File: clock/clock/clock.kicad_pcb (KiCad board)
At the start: 2 copper layers, 43 parts, among them J1 AVR-ISP-6, J10 Conn_01x05_Male, J11 Conn_01x05_Male, J12 Conn_01x05_Male, J13 Conn_01x05_Male, J2 EURORACK_CONN_10, J3 CV_IN, J4 CLOCK_OUT, J5 SUBDIV_OUT, J6 Conn_01x05_Female, J7 Conn_01x05_Female, J8 Conn_01x05_Female, J9 Conn_01x05_Female, SW1 SW_Push, SW2 SW_Push, SW3 SW_Rotary8, U1 ATmega328P-PU, U2 L7805, U3 SM460281N, U4 SM460281N, U5 SM460281N, Y1 16MHz

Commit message: pcb layout first pass
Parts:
- removed the J10 at (1.91, 32.4)
- removed the J11 at (1.91, 46.4)
- removed the J12 at (1.91, 60.3)
- added J3: Conn_01x05_Female, Connector_PinSocket_2.54mm:PinSocket_1x05_P2.54mm_Vertical, F.Cu at (42.0, 33.5)
- added J4: Conn_01x05_Male, Connector_PinHeader_2.54mm:PinHeader_1x05_P2.54mm_Vertical, B.Cu at (2.00, 33.5)
- added J5: Conn_01x05_Female, Connector_PinSocket_2.54mm:PinSocket_1x05_P2.54mm_Vertical, F.Cu at (42.0, 48.8)
- J6, J8: value Conn_01x05_Female -> Conn_01x05_Male; footprint Connector_PinSocket_2.54mm:PinSocket_1x05_P2.54mm_Vertical -> Connector_PinHeader_2.54mm:PinHeader_1x05_P2.54mm_Vertical; moved to B.Cu
- moved R5 113.7 mm to (7.49, 100.7), turned to 180 degrees
- moved R4 111.0 mm to (13.0, 100.7), turned to 180 degrees
- moved C3 70.2 mm to (42.5, 25.0), turned to 270 degrees
- moved C1 64.4 mm to (43.0, 80.8), turned to 90 degrees
- moved J1 62.5 mm to (52.8, 84.0)
- moved R15 62.2 mm to (46.5, 38.0)
- moved R14 58.9 mm to (46.5, 34.5)
- moved R13 56.3 mm to (46.5, 31.0)
- moved C4 53.9 mm to (48.5, 27.0)
- moved J9 49.4 mm to (42.0, 97.8)
- moved J8 48.5 mm to (2.00, 64.0), turned to 180 degrees
- moved R1 41.7 mm to (42.0, 84.0)
- moved C2 40.9 mm to (52.8, 79.2), turned to 180 degrees
- moved U1 39.0 mm to (45.5, 41.5)
- moved Y1 37.6 mm to (52.5, 33.0), turned to 270 degrees
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- renumbered J13 to J10, J3 to J11, J4 to J12, J5 to J13
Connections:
- J10 pad 3: /LED_A -> /AVCC
- J10 pad 4: /LED_B -> /AGND
- J13 pad S: /AGND -> Net-(J13-PadS)
- J6 pad 1: /B_CLOCK_OUT -> /LED2
- J6 pad 2: /B_SUBDIV_OUT -> /LED_C2
- J6 pad 3: /B_CV_IN -> /LED1
- J6 pad 4: /B_LED0 -> /LED3
- J6 pad 5: /B_LED1 -> /LED_C3
- J7 pad 1: /B_LED2 -> /B_LED4
- J7 pad 2: /B_LED3 -> /B_LED5
- J7 pad 3: /B_LED4 -> /B_LED6
- J7 pad 4: /B_LED5 -> /B_LED_A
- J7 pad 5: /B_LED6 -> /B_LED_B
- J8 pad 1: /B_LED_C1 -> /LED4
- J8 pad 2: /B_LED_C2 -> /LED5
- J8 pad 3: /B_LED_C3 -> /LED6
- J8 pad 4: +5V -> /LED_A
- J8 pad 5: GND -> /LED_B
- J9 pad 3: /B_LED_A -> +5V
- J9 pad 4: /B_LED_B -> GND
- R4 pad 2: GND -> /AGND
- R5 pad 2: GND -> /AGND
- U4 pad 2: /LED1 -> /LED2
- U4 pad 4: /LED2 -> /LED1
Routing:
- net /B_SUBDIV_OUT: track 0.00 -> 76.2 mm, vias 0 -> 1
- net +5V: track 0.00 -> 71.3 mm
- net /B_KNOB: track 0.00 -> 52.2 mm
- net /B_CLOCK_OUT: track 0.00 -> 51.6 mm
- net /~RESET: track 0.00 -> 51.6 mm, vias 0 -> 1
- net /LED_A: track 0.00 -> 46.3 mm
- net Net-(C3-Pad2): track 0.00 -> 44.2 mm
- net /B_SW2: track 0.00 -> 43.8 mm
- net Net-(C4-Pad2): track 0.00 -> 41.3 mm
- net /AVCC: track 57.4 -> 97.7 mm
- net /B_LED_A: track 0.00 -> 37.1 mm
- net /LED_B: track 0.00 -> 35.8 mm
- net /B_SW1: track 0.00 -> 29.2 mm
- net /LED1: track 4.00 -> 28.6 mm
- net /LED2: track 4.23 -> 28.8 mm
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- added copper zone on B.Cu, net GND
- added copper zone on F.Cu, net GND
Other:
- board text added: "TODO: power connector orientation?"
- board text added: "TODO: silkscreen"
- board text added: "TODO: switch connector sides for stability?"

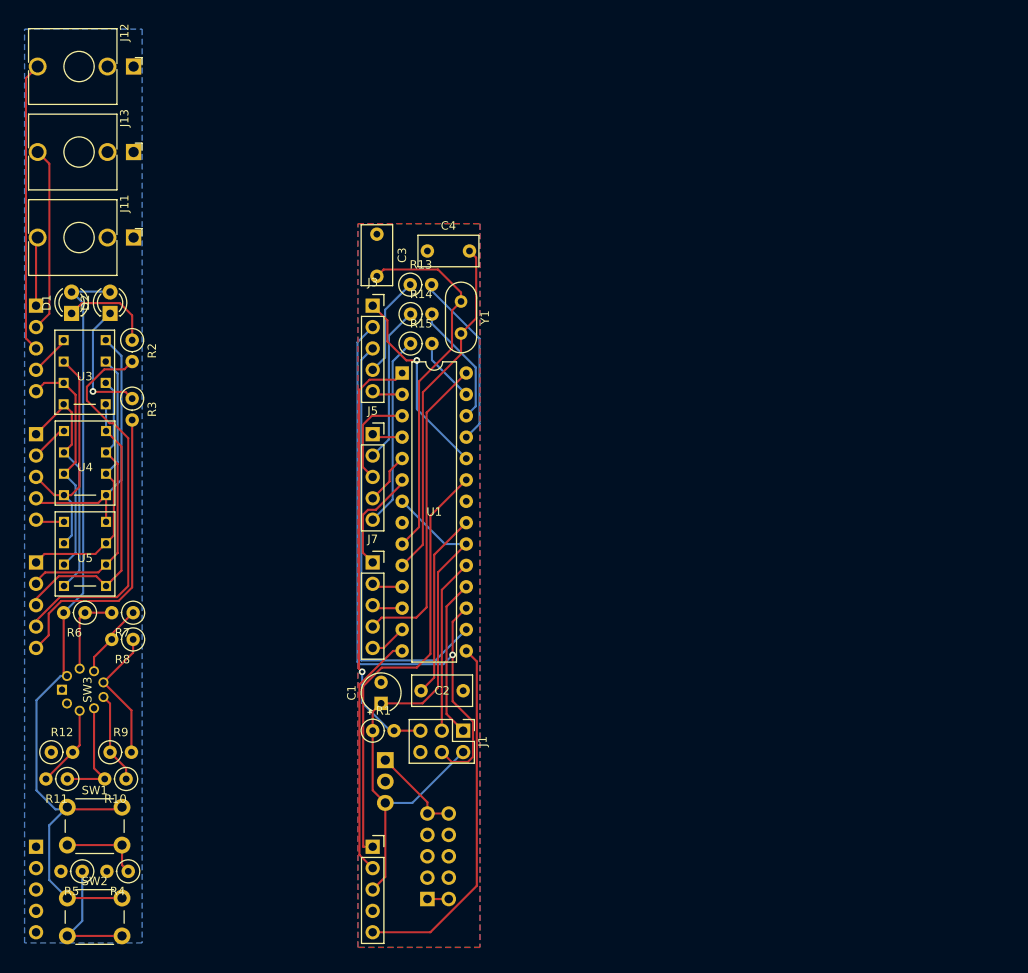
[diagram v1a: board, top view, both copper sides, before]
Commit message: cleanup pcb and silkscreen
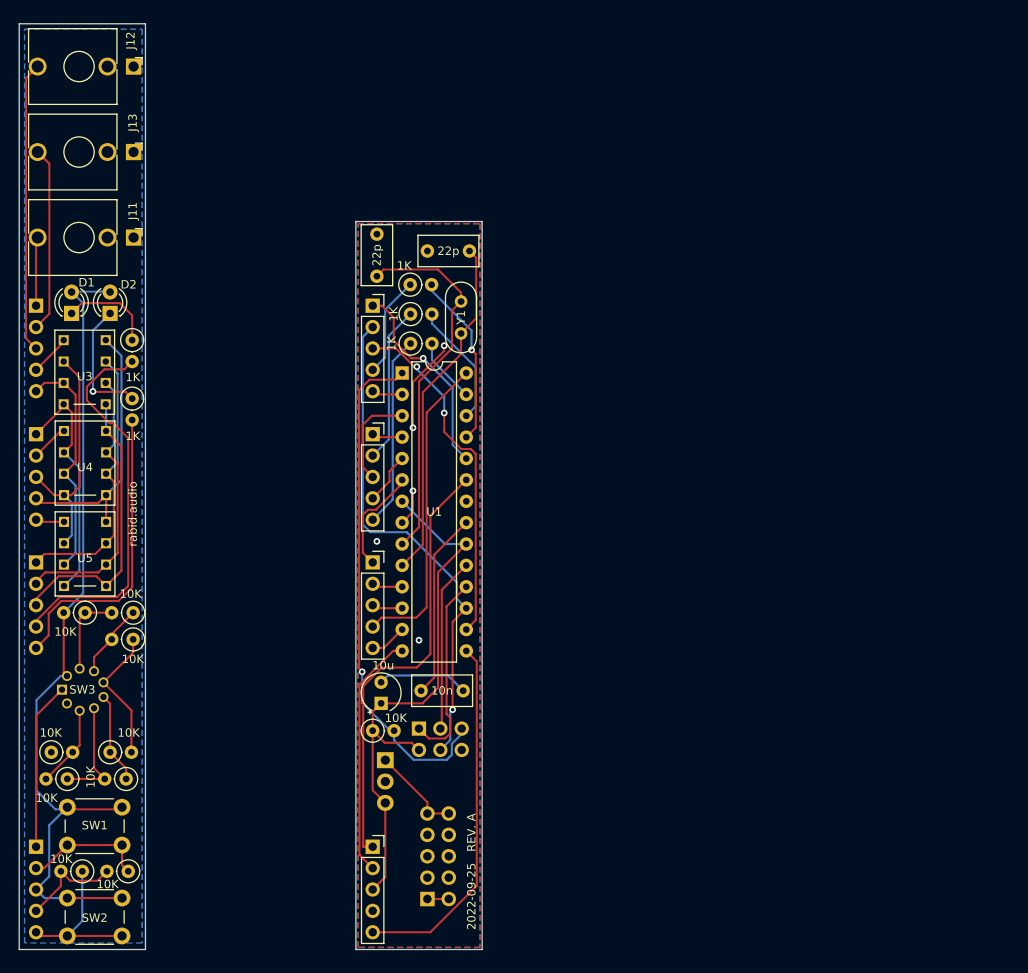
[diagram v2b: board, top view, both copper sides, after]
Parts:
- J1: value AVR-ISP-6 -> AVR-ISP; moved to B.Cu
- moved J1 5.26 mm to (47.5, 83.8)
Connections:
- J11 pad TN: (no net) -> /AGND
- J12 pad TN: (no net) -> Net-(J12-PadTN)
- J13 pad S: Net-(J13-PadS) -> /AGND
- J13 pad TN: (no net) -> Net-(J13-PadTN)
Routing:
- net GND: track 0.00 -> 26.4 mm, vias 0 -> 5
- net /KNOB: track 0.00 -> 19.9 mm
- net /B_SUBDIV_OUT: track 76.2 -> 59.6 mm
- net /AGND: track 0.00 -> 12.3 mm
- net /B_CLOCK_OUT: track 51.6 -> 41.4 mm, vias 0 -> 2
- net /~RESET: track 51.6 -> 61.2 mm
- net +5V: track 71.3 -> 66.0 mm
- net /SW1: track 9.93 -> 14.8 mm
- net /MISO: track 18.9 -> 23.0 mm
- net /SW2: track 15.5 -> 19.4 mm
- net /AVCC: track 97.7 -> 100.5 mm
- net /B_CV_IN: track 24.2 -> 24.9 mm
- net Net-(R13-Pad2): track 21.1 -> 20.8 mm, vias 0 -> 1
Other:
- board outline added: 55 x 110 mm
- board text added: "2022-09-25 REV. A"
- board text added: "TODO: confirm pot orientation"
- board text added: "TODO: confirm switches"
- board text added: "rabid.audio"
- board text removed: "TODO: silkscreen"

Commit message: update pcb
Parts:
- removed the R6 at (7.82, 70.0)
- removed the R8 at (13.5, 73.2)
- added D3: 1N4148, Diode_THT:D_T-1_P5.08mm_Horizontal, B.Cu at (7.33, 18.5)
- added R13: 68k, Resistor_THT:R_Axial_DIN0207_L6.3mm_D2.5mm_P2.54mm_Vertical, F.Cu at (5.25, 89.2)
- added R15: 100K, Resistor_THT:R_Axial_DIN0207_L6.3mm_D2.5mm_P7.62mm_Horizontal, B.Cu at (6.00, 22.0)
- J1: value AVR-ISP -> AVR-ISP-6
- R10: value 10K -> 220K
- R11: value 10K -> 470K
- R12: value 10K -> 1M
- R14: value 1K -> 180K; footprint Resistor_THT:R_Axial_DIN0207_L6.3mm_D2.5mm_P2.54mm_Vertical -> Resistor_THT:R_Axial_DIN0207_L6.3mm_D2.5mm_P7.62mm_Horizontal; moved to B.Cu
- R7: value 10K -> 1K
- R9: value 10K -> 120K
- SW3: value SW_Rotary8 -> SW_Coded_SH-7050; footprint synth:RM100772BCB -> synth:SD-1110
- moved R7 48.4 mm to (46.5, 34.5), turned to 0 degrees
- moved R14 37.1 mm to (9.87, 28.8), turned to 180 degrees
- moved R10 18.1 mm to (11.0, 71.8), turned to 270 degrees
- moved R12 15.1 mm to (6.50, 71.8), turned to 270 degrees
- moved R9 11.2 mm to (2.00, 93.5), turned to 90 degrees
- moved R11 7.30 mm to (13.0, 89.2)
- moved R8 6.75 mm to (46.5, 31.2)
- moved R6 6.75 mm to (46.5, 37.8)
- moved SW3 2.62 mm to (7.75, 81.8), turned to 0 degrees
- renumbered R13 to R6, R15 to R8
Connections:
- J11 pad T: /CV_IN -> Net-(D3-Pad2)
- R10 pad 1: Net-(R10-Pad1) -> /AVCC
- R11 pad 1: Net-(R10-Pad2) -> /AVCC
- R12 pad 1: /AGND -> /AVCC
- R12 pad 2: Net-(R11-Pad2) -> Net-(R12-Pad2)
- R14 pad 1: /B_LED_C2 -> Net-(D3-Pad1)
- R14 pad 2: Net-(R14-Pad2) -> /CV_IN
- R6 pad 1: /B_LED_C1 -> /B_LED_C3
- R6 pad 2: Net-(R13-Pad2) -> Net-(R6-Pad2)
- R7 pad 1: Net-(R7-Pad1) -> /B_LED_C2
- R7 pad 2: Net-(R6-Pad1) -> Net-(R7-Pad2)
- R8 pad 1: /B_LED_C3 -> /B_LED_C1
- R8 pad 2: Net-(R15-Pad2) -> Net-(R8-Pad2)
- R9 pad 1: Net-(R10-Pad1) -> /AVCC
- R9 pad 2: Net-(R8-Pad1) -> Net-(R9-Pad2)
- SW3 pad 1: /AVCC -> Net-(R9-Pad2)
- SW3 pad 2: Net-(R6-Pad1) -> Net-(R10-Pad2)
- SW3 pad 4: Net-(R8-Pad1) -> Net-(R11-Pad2)
- SW3 pad 8: /AGND -> Net-(R12-Pad2)
- U1 pad 25: Net-(R13-Pad2) -> /B_LED_A
- U1 pad 26: Net-(R14-Pad2) -> Net-(R6-Pad2)
- U1 pad 27: Net-(R15-Pad2) -> Net-(R7-Pad2)
- U1 pad 28: /B_LED_A -> Net-(R8-Pad2)
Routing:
- net Net-(R13-Pad2): track 20.8 -> 0.00 mm, vias 1 -> 0
- net Net-(R8-Pad1): track 16.2 -> 0.00 mm
- net Net-(R14-Pad2): track 14.7 -> 0.00 mm
- net Net-(R8-Pad2): track 0.00 -> 13.2 mm
- net Net-(D3-Pad1): track 0.00 -> 11.3 mm
- net Net-(R7-Pad2): track 0.00 -> 11.2 mm
- net Net-(R10-Pad1): track 10.9 -> 0.00 mm
- net Net-(R6-Pad1): track 10.7 -> 0.00 mm
- net Net-(R6-Pad2): track 0.00 -> 10.5 mm
- net Net-(R10-Pad2): track 13.0 -> 3.94 mm
- net Net-(R7-Pad1): track 8.87 -> 0.00 mm
- net /B_LED_A: track 37.1 -> 28.9 mm
- net Net-(R15-Pad2): track 7.73 -> 0.00 mm
- net Net-(D3-Pad2): track 0.00 -> 6.93 mm
- net Net-(R9-Pad2): track 0.00 -> 6.73 mm
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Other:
- board text removed: "TODO: confirm switches"
- board text removed: "TODO: power connector orientation?"
- board text removed: "TODO: switch connector sides for stability?"

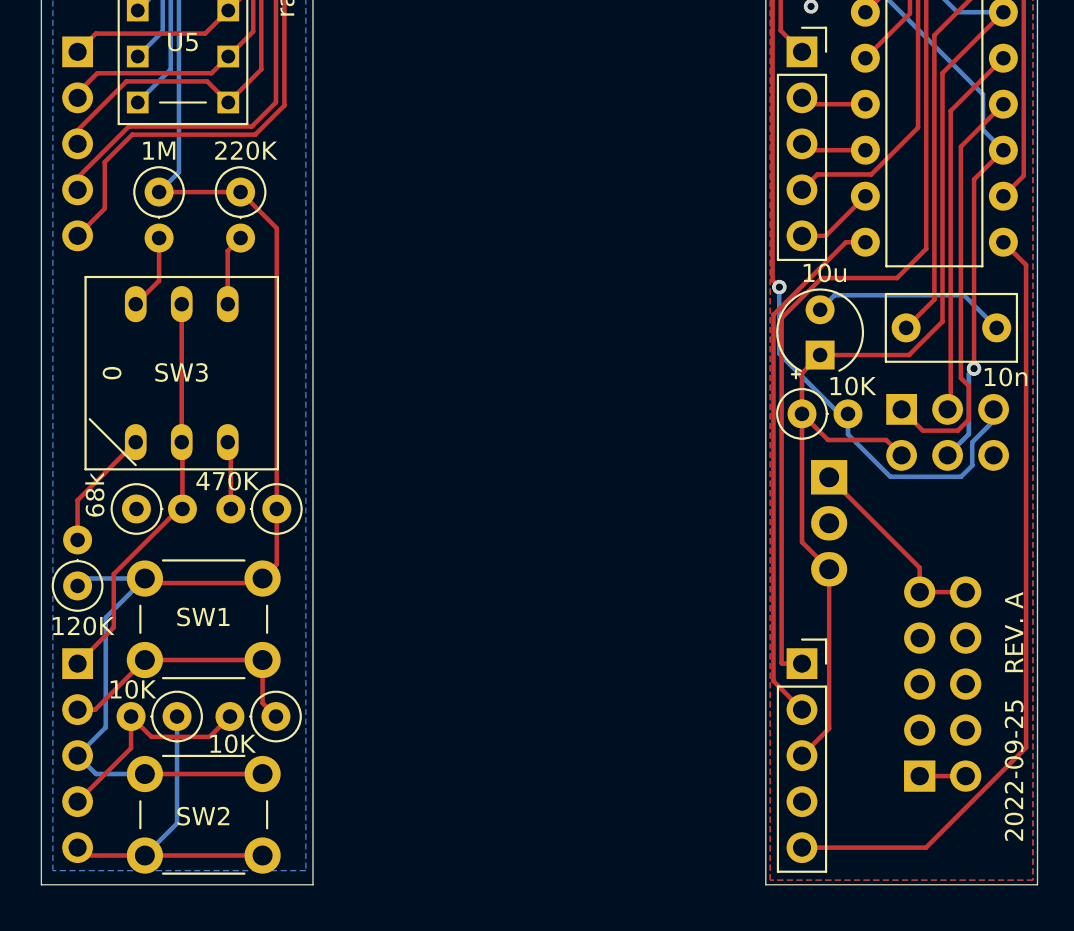
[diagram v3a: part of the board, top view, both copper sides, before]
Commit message: switch side of bottom header for structural support
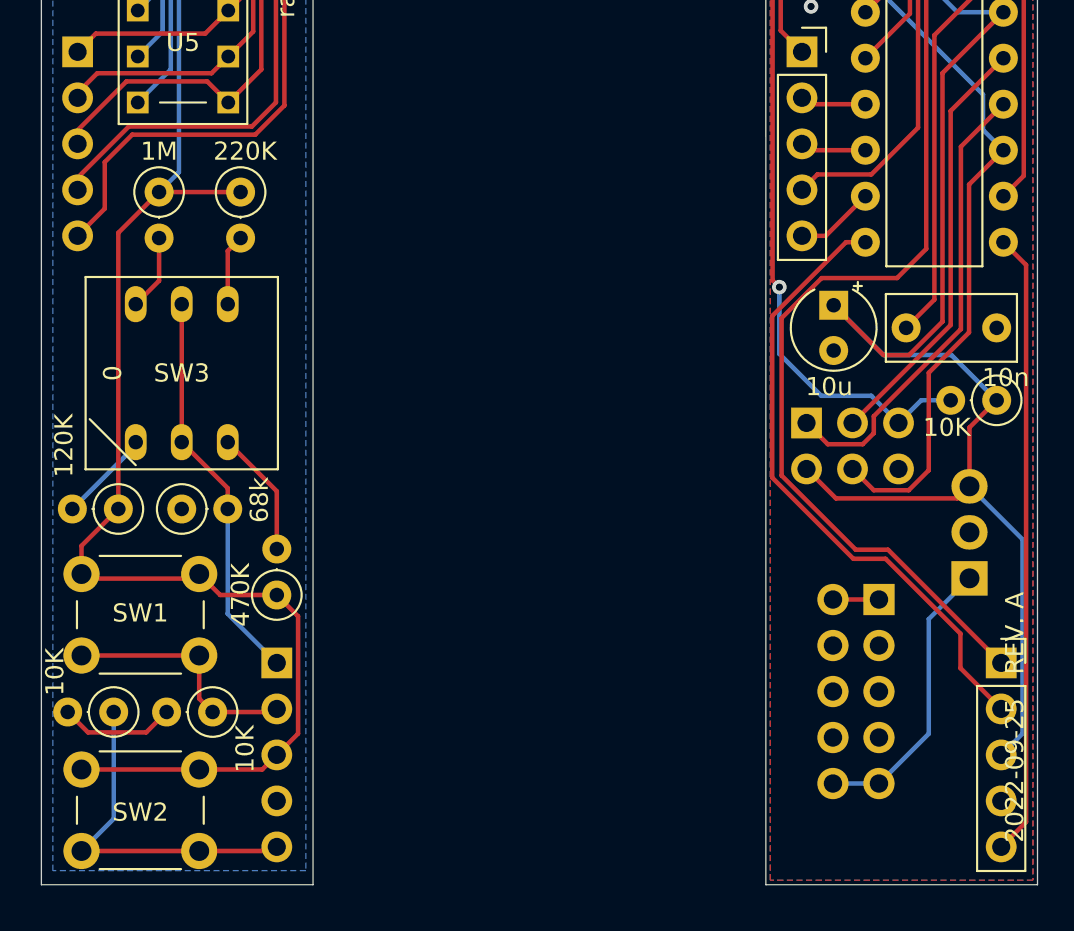
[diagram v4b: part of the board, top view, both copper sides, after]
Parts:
- moved J10 11.0 mm to (13.0, 97.8)
- moved J9 11.0 mm to (53.0, 97.8)
- moved R1 10.8 mm to (52.8, 83.2), turned to 180 degrees
- moved J2 10.0 mm to (46.2, 94.2), turned to 180 degrees
- moved U2 9.55 mm to (51.2, 93.1), turned to 90 degrees
- moved J1 5.30 mm to (42.2, 84.5)
- moved R9 4.81 mm to (4.25, 89.2), turned to 180 degrees
- moved R11 4.75 mm to (13.0, 94.0), turned to 90 degrees
- moved R5 3.51 mm to (3.99, 100.5)
- moved R4 3.51 mm to (9.45, 100.5)
- moved SW1 3.51 mm to (2.21, 92.8)
- moved SW2 3.51 mm to (2.21, 103.6)
- moved C1 2.85 mm to (43.8, 78.0), turned to 270 degrees
- moved R13 2.50 mm to (7.75, 89.2)
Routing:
- net +5V: track 66.0 -> 79.1 mm
- net GND: track 26.4 -> 15.6 mm
- net /B_SW2: track 43.8 -> 35.2 mm
- net /B_SUBDIV_OUT: track 59.6 -> 66.0 mm, vias 1 -> 0
- net /AGND: track 12.3 -> 6.39 mm
- net /~RESET: track 61.2 -> 55.5 mm
- net /B_SW1: track 29.2 -> 34.8 mm
- net Net-(J2-Pad9): track 11.0 -> 15.9 mm
- net /B_KNOB: track 52.2 -> 57.1 mm
- net Net-(R11-Pad2): track 3.76 -> 7.26 mm
- net /SCK: track 20.7 -> 23.6 mm
- net /MISO: track 23.0 -> 25.6 mm
- net Net-(R9-Pad2): track 6.73 -> 5.33 mm
- net /SW1: track 14.8 -> 13.5 mm
